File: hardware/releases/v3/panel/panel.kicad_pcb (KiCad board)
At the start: 4 copper layers, 65.9 x 78 mm, 125 parts, among them J1 KNX bus terminal pins, J101 Carrier, J102 OLED, J2 AUX 20-32 V (yellow/white), J3 DALI bus (push-in), J4 UI board, Q1 MJD45H11, Q2 BC857, Q3 IRLML0060, Q4 BC847, Q5 BC847, Q6 BC847, SW101 PRG/RST, SW102 FUNC, U1 NCN5130MNTWG, U10 TPS2121RUXR, U101 74AHCT1G125, U2 SCT2400TVBR, U3 REC3-2415SRW/H2/A/CTRL 24V->1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, U4 TLP383, U5 TLP383(D4BLLTL,E, U6 TLP383(D4BLLTL,E, U7 LM66100, U8 XIAO ESP32C6, U9 TMR 2411 24V->5V 2W iso, Y1 16MHz

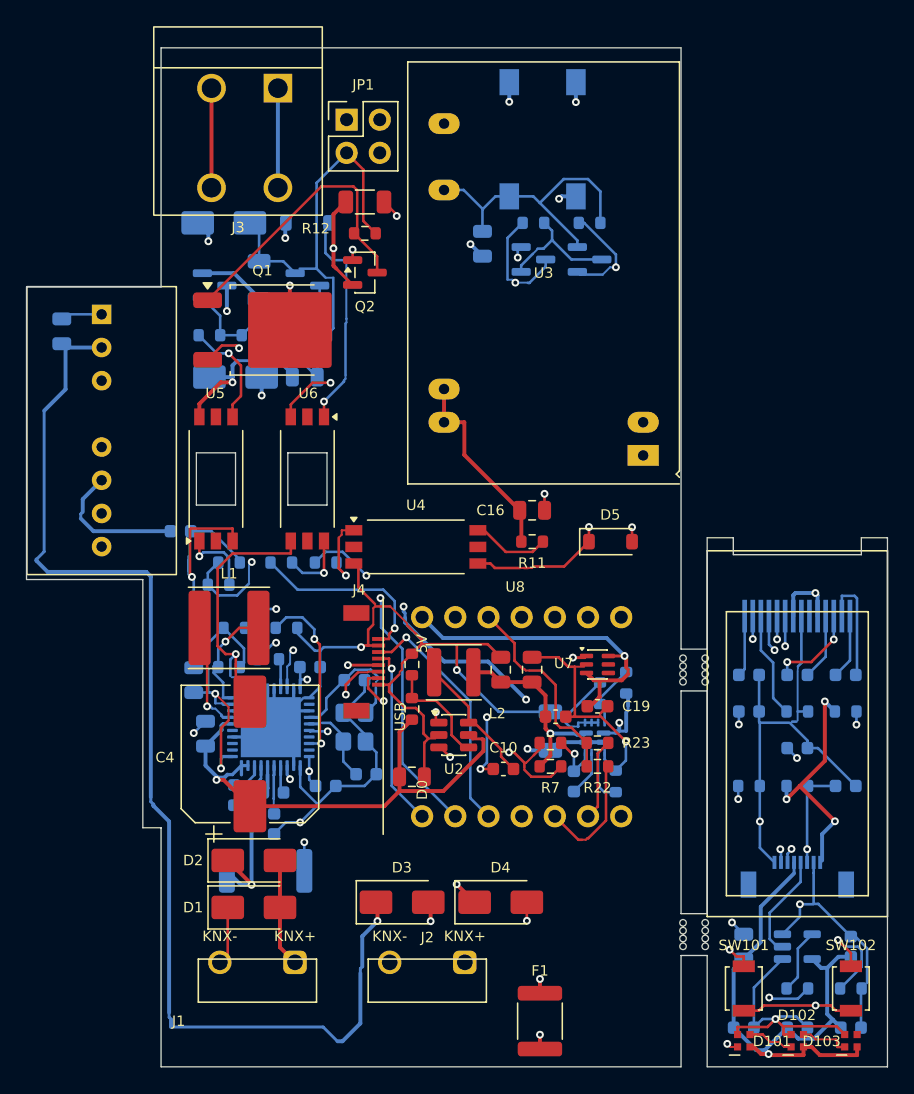
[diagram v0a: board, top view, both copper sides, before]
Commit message: Added zero-length track segments to fix hairline joints where track ends grazed pads instead of fully entering them
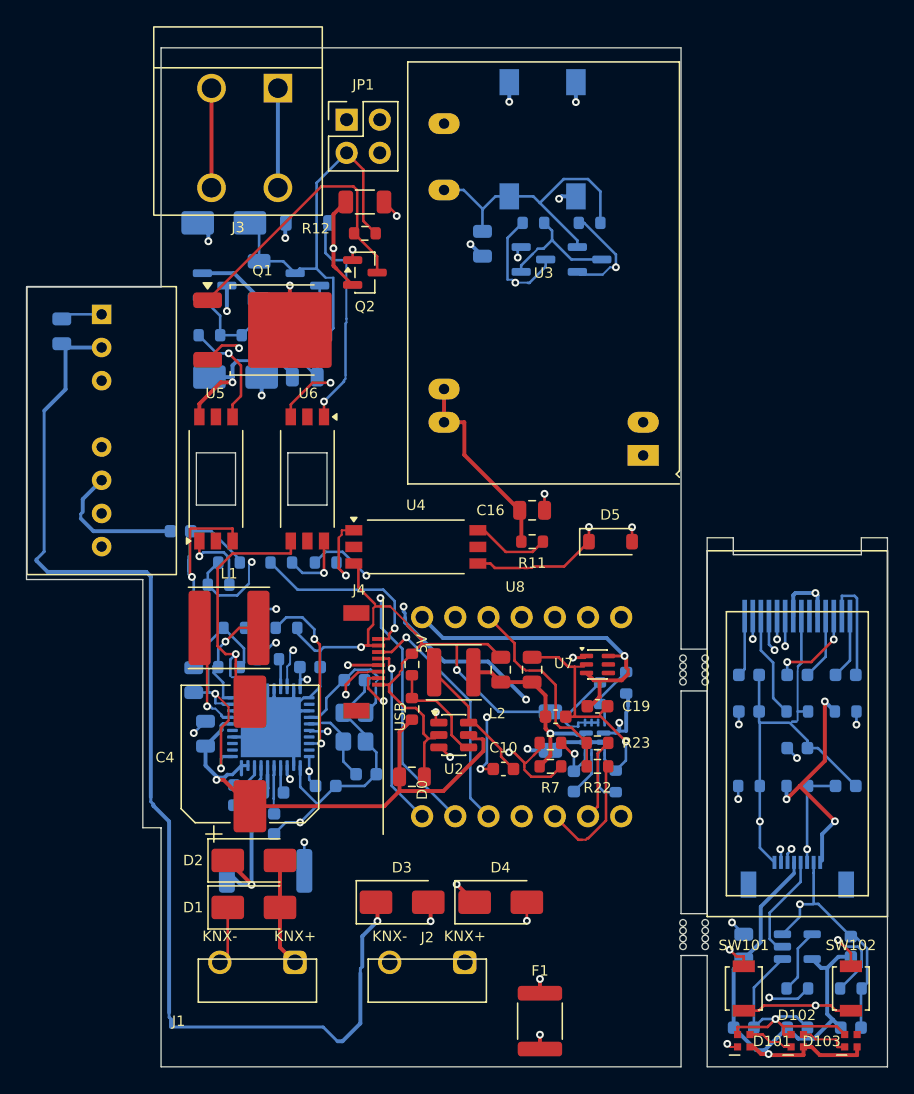
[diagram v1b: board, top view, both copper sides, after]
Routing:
- net GND: track 159.6 -> 175.7 mm
- net UI_GND: track 74.0 -> 74.6 mm
